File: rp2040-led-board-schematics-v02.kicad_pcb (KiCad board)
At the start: 4 copper layers, 228 x 98 mm, 293 parts, among them J1 ReceiverRS485, J10 Terminal, J11 ReceiverData, J12 ReceiverData, J13 ReceiverData, J14 ReceiverData, J15 ReceiverRS485, J16 ReceiverRS485, J17 ReceiverRS485, J18 ReceiverRS485, J19 Terminal, J2 ReceiverRS485, J20 Terminal, J21 Terminal, J22 Terminal, J23 ReceiverData, J24 ReceiverData, J25 ReceiverData, J26 ReceiverData, J27 MainBoard, J3 ReceiverRS485, J4 ReceiverRS485, J5 PWR_IN, J6 Terminal, J7 Terminal, J8 Terminal, J9 FrontPanel, Q1 AO3401A, SW1 PEC16, SW2 Button, U10 MAX485EE, U11 MAX485EE, U12 MAX485EE, U13 MAX485EE, U14 Pico, U15 MAX485EE, U16 MAX485EE, U17 AMS1117-5.0, U2 LMR50410Y5FQDBVRQ1, U21 MAX485EE, U22 MAX485EE, U23 MAX485EE, U24 MAX485EE, U25 MAX485EE, U26 MAX485EE, U27 ENC28J60, U29 AMS1117-5.0, U30 AMS1117-5.0, U31 AMS1117-5.0, U32 AMS1117-5.0, U33 AMS1117-5.0, U34 AMS1117-5.0, U35 AMS1117-5.0, U6 MAX485EE, U7 MAX485EE, U8 MAX485EE, U9 MAX485EE

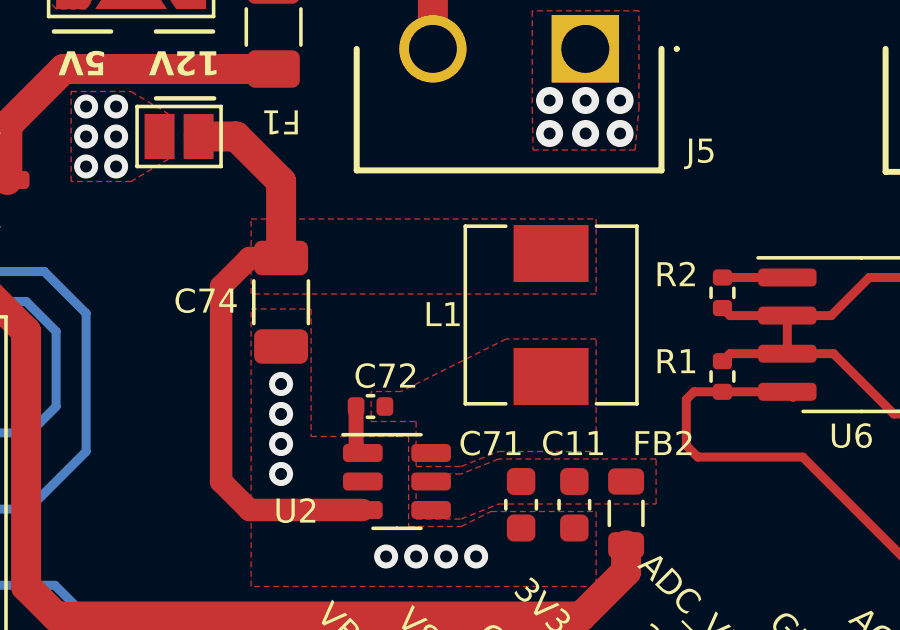
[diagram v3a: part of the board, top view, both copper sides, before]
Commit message: JLCPCB pluging assignation done
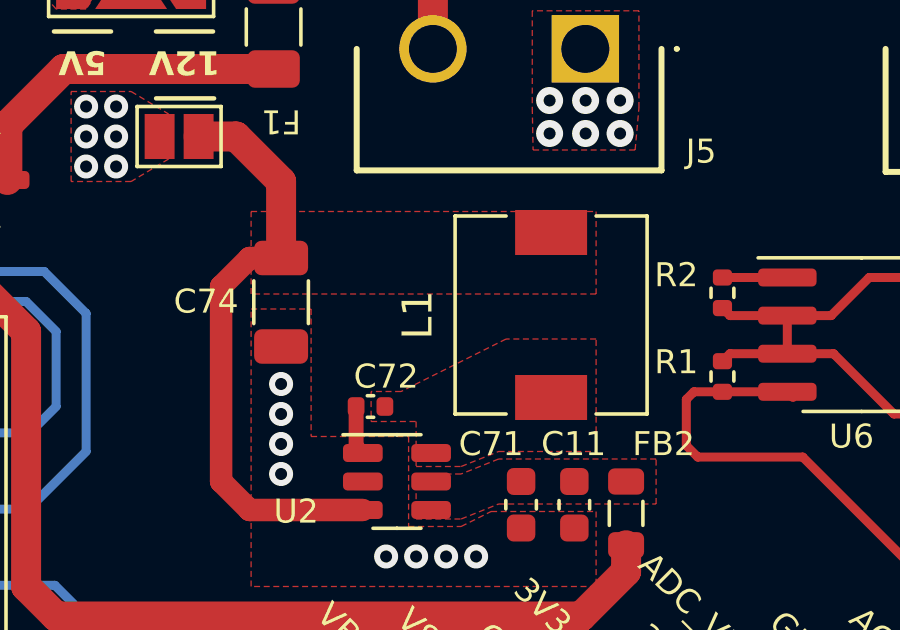
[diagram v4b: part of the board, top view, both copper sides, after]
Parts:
- L1: footprint Inductor_SMD:L_Sunlord_MWSA0503S -> Inductor_SMD:L_6.3x6.3_H3
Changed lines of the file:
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@@
     )
   )
-  (footprint "Inductor_SMD:L_Sunlord_MWSA0503S" (layer "F.Cu")
+  (footprint "Inductor_SMD:L_6.3x6.3_H3" (layer "F.Cu")
     (at 69 73.95 90)
-    (descr "Inductor, Sunlord, MWSA0503S, 5.4x5.2x2.8mm, https://sunlordinc.com/Download.aspx?file=L1VwbG9hZEZpbGVzL1BERl9DYXQvMjAyMjExMTUxNDQ4MDU0NTQucGRm&lan=en")
-    (tags "Inductor mwsa")
+    (descr "Choke, SMD, 6.3x6.3mm 3mm height")
+    (tags "Choke SMD")
     (property "Sheetfile" "rp2040-led-board-schematics-v02.kicad_sch")
     (property "Sheetname" "")
@@
     (property "ki_keywords" "inductor choke coil reactor magnetic")
     (attr smd)
-    (fp_text reference "L1" (at 0 -3.6 180) (layer "F.SilkS")
-        (effects (font (size 0.8 0.8) (thickness 0.15)))
+    (fp_text reference "L1" (at 0 -4.45 90) (layer "F.SilkS")
+        (effects (font (size 1 1) (thickness 0.15)))
     )
-    (fp_text value "5.6mH 120mOhm" (at 0 3.6 90) (layer "F.Fab")
-        (effects (font (size 0.8 0.8) (thickness 0.15)))
+    (fp_text value "5.6mH 120mOhm" (at 0 4.45 90) (layer "F.Fab")
+        (effects (font (size 1 1) (thickness 0.15)))
     )
     (fp_text user "${REFERENCE}" (at 0 0 90) (layer "F.Fab")
-        (effects (font (size 0.8 0.8) (thickness 0.15)))
+        (effects (font (size 1 1) (thickness 0.15)))
     )
-    (fp_line (start -2.96 -2.86) (end -2.96 -1.51)
+    (fp_line (start -3.3 -3.2) (end 3.3 -3.2)
       (stroke (width 0.12) (type solid)) (layer "F.SilkS"))
-    (fp_line (start -2.96 -2.86) (end 2.96 -2.86)
+    (fp_line (start -3.3 -1.5) (end -3.3 -3.2)
       (stroke (width 0.12) (type solid)) (layer "F.SilkS"))
-    (fp_line (start -2.96 2.86) (end -2.96 1.51)
+    (fp_line (start -3.3 3.2) (end -3.3 1.5)
       (stroke (width 0.12) (type solid)) (layer "F.SilkS"))
-    (fp_line (start -2.96 2.86) (end 2.96 2.86)
+    (fp_line (start 3.3 -3.2) (end 3.3 -1.5)
       (stroke (width 0.12) (type solid)) (layer "F.SilkS"))
-    (fp_line (start 2.96 -2.86) (end 2.96 -1.51)
+    (fp_line (start 3.3 1.5) (end 3.3 3.2)
       (stroke (width 0.12) (type solid)) (layer "F.SilkS"))
-    (fp_line (start 2.96 2.86) (end 2.96 1.51)
+    (fp_line (start 3.3 3.2) (end -3.3 3.2)
       (stroke (width 0.12) (type solid)) (layer "F.SilkS"))
-    (fp_line (start -3.25 -2.85) (end -3.25 2.85)
+    (fp_line (start -3.75 -3.4) (end -3.75 3.4)
       (stroke (width 0.05) (type solid)) (layer "F.CrtYd"))
-    (fp_line (start -3.25 2.85) (end 3.25 2.85)
+    (fp_line (start -3.75 3.4) (end 3.75 3.4)
       (stroke (width 0.05) (type solid)) (layer "F.CrtYd"))
-    (fp_line (start 3.25 -2.85) (end -3.25 -2.85)
+    (fp_line (start 3.75 -3.4) (end -3.75 -3.4)
       (stroke (width 0.05) (type solid)) (layer "F.CrtYd"))
-    (fp_line (start 3.25 2.85) (end 3.25 -2.85)
+    (fp_line (start 3.75 3.4) (end 3.75 -3.4)
       (stroke (width 0.05) (type solid)) (layer "F.CrtYd"))
-    (fp_line (start -2.7 -2.6) (end -2.7 2.6)
+    (fp_line (start -3.15 -3.15) (end -3.15 -1.5)
+      (stroke (width 0.1) (type solid)) (layer "F.Fab"))
+    (fp_line (start -3.15 -3.15) (end 3.15 -3.15)
+      (stroke (width 0.1) (type solid)) (layer "F.Fab"))
+    (fp_line (start -3.15 3.15) (end -3.15 1.5)
+      (stroke (width 0.1) (type solid)) (layer "F.Fab"))
+    (fp_line (start -3.15 3.15) (end 3.15 3.15)
+      (stroke (width 0.1) (type solid)) (layer "F.Fab"))
+    (fp_line (start 3.15 -3.15) (end 3.15 -1.5)
       (stroke (width 0.1) (type solid)) (layer "F.Fab"))
-    (fp_line (start -2.7 2.6) (end 2.7 2.6)
+    (fp_line (start 3.15 3.15) (end 3.15 1.5)
       (stroke (width 0.1) (type solid)) (layer "F.Fab"))
-    (fp_line (start 2.7 -2.6) (end -2.7 -2.6)
+    (fp_arc (start -1.91 -1.91) (mid 0 -2.701148) (end 1.91 -1.91)
       (stroke (width 0.1) (type solid)) (layer "F.Fab"))
-    (fp_line (start 2.7 2.6) (end 2.7 -2.6)
+    (fp_arc (start 1.91 1.91) (mid 0 2.701148) (end -1.91 1.91)
       (stroke (width 0.1) (type solid)) (layer "F.Fab"))
-    (pad "1" smd rect (at -2.05 0 90) (size 1.9 2.5) (layers "F.Cu" "F.Paste" "F.Mask")
+    (pad "1" smd rect (at -2.75 0 90) (size 1.5 2.4) (layers "F.Cu" "F.Paste" "F.Mask")
       (net 162 "/SW") (pintype "passive"))
-    (pad "2" smd rect (at 2.05 0 90) (size 1.9 2.5) (layers "F.Cu" "F.Paste" "F.Mask")
+    (pad "2" smd rect (at 2.75 0 90) (size 1.5 2.4) (layers "F.Cu" "F.Paste" "F.Mask")
       (net 159 "/Buck out") (pintype "passive"))
-    (model "${KICAD7_3DMODEL_DIR}/Inductor_SMD.3dshapes/L_Sunlord_MWSA0503S.wrl"
+    (model "${KICAD6_3DMODEL_DIR}/Inductor_SMD.3dshapes/L_6.3x6.3_H3.wrl"
       (offset (xyz 0 0 0))
       (scale (xyz 1 1 1))
@@
     (fp_line (start 1.6 0.8) (end -1.6 0.8)
       (stroke (width 0.1) (type solid)) (layer "F.Fab"))
-    (pad "1" smd roundrect (at -1.475 0 270) (size 1.15 1.8) (layers "F.Cu" "F.Paste" "F.Mask") (roundrect_rratio 0.217391)
+    (pad "1" smd roundrect (at -1.475 0 270) (size 1.15 1.8) (layers "F.Cu" "F.Paste" "F.Mask") (roundrect_rratio 0.2173913043)
       (net 159 "/Buck out") (pintype "passive"))
-    (pad "2" smd roundrect (at 1.475 0 270) (size 1.15 1.8) (layers "F.Cu" "F.Paste" "F.Mask") (roundrect_rratio 0.217391)
+    (pad "2" smd roundrect (at 1.475 0 270) (size 1.15 1.8) (layers "F.Cu" "F.Paste" "F.Mask") (roundrect_rratio 0.2173913043)
       (net 2 "GND") (pintype "passive"))
     (model "${KICAD6_3DMODEL_DIR}/Capacitor_SMD.3dshapes/C_1206_3216Metric.wrl"
@@
     (polygon
       (pts
-        (xy 59 70.75)
-        (xy 70.5 70.75)
+        (xy 59 70.5)
+        (xy 70.5 70.5)
         (xy 70.5 73.25)
         (xy 59 73.25)
